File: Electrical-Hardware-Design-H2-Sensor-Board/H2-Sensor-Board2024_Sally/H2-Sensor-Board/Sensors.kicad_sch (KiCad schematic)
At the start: 28 parts, among them J4 Conn_01x03, J5 Conn_01x03, J6 Conn_01x03, J7 Conn_01x03, SW2 TARE BUTTON, U8 AD8608ARZ, U9 BME280

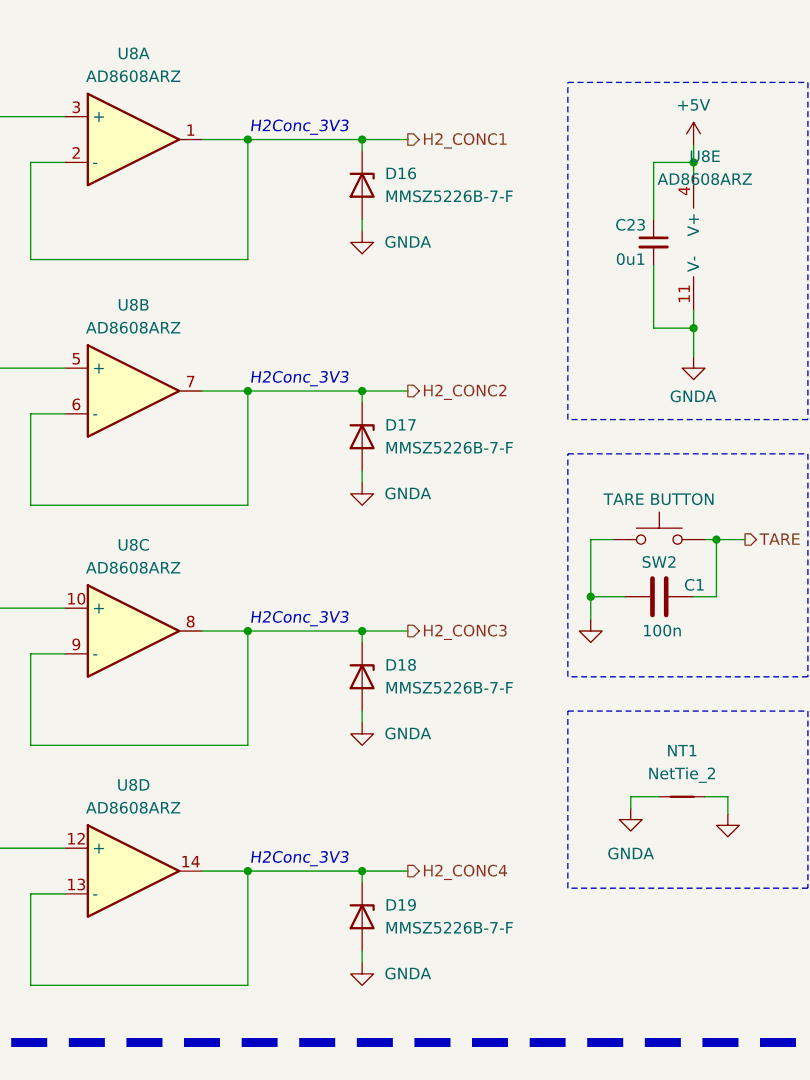
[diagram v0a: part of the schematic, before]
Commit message: reworked comparator+ADC pinout, added terminal C bank
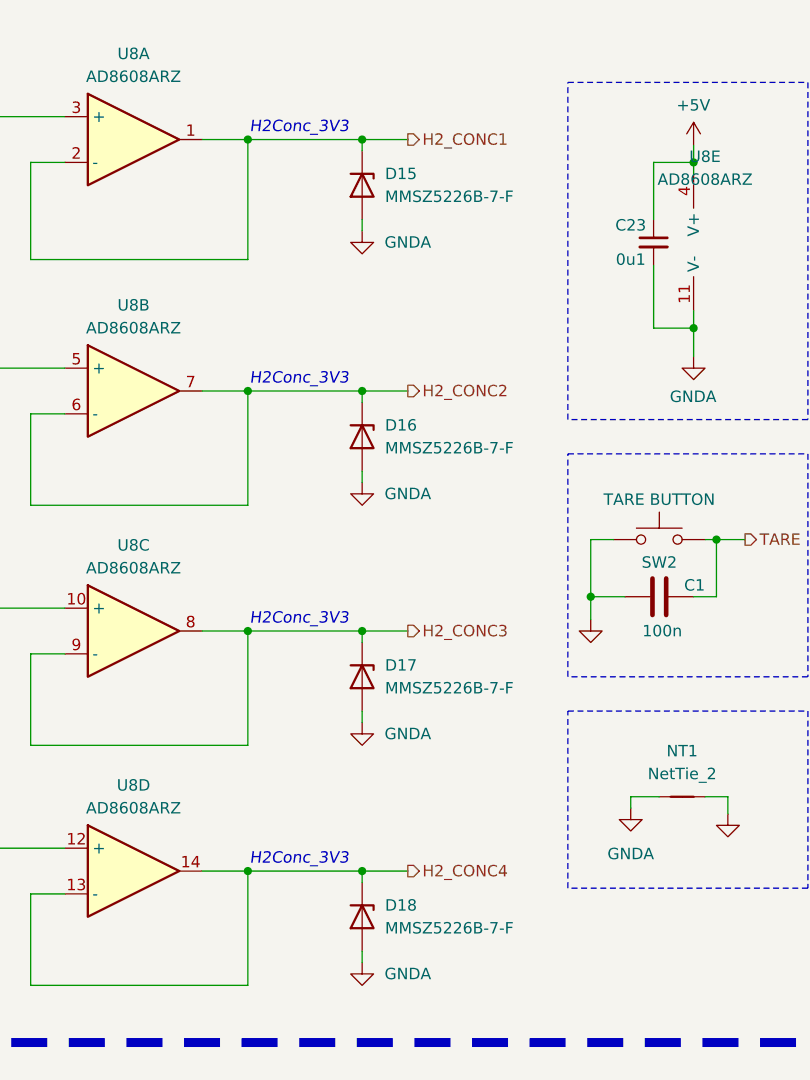
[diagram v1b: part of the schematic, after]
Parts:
- renumbered D16 to D15, D17 to D16, D18 to D17, D19 to D18
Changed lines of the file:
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@@
 		(on_board yes)
 		(dnp no)
-		(property "Reference" "#PWR044"
+		(property "Reference" "#PWR039"
 			(at 121.285 115.57 0)
 			(effects
@@
 			(project "H2 Sensor Board Lucy Rev 1"
 				(path "/61fdd4a1-2d1e-44dc-8644-252e12d35745/7173564b-4ce8-4fe4-9cf3-378e96487dfe"
-					(reference "#PWR044")
+					(reference "#PWR039")
 					(unit 1)
 				)
@@
 		(dnp no)
 		(fields_autoplaced yes)
-		(property "Reference" "D17"
+		(property "Reference" "D16"
 			(at 93.98 66.675 90)
 			(effects
@@
 			(project "H2-Sensor-Board_Sally-R1.0"
 				(path "/61fdd4a1-2d1e-44dc-8644-252e12d35745/7173564b-4ce8-4fe4-9cf3-378e96487dfe"
-					(reference "D17")
+					(reference "D16")
 					(unit 1)
 				)
@@
 		(on_board yes)
 		(dnp no)
-		(property "Reference" "#PWR035"
+		(property "Reference" "#PWR030"
 			(at 43.18 51.435 0)
 			(effects
@@
 			(project "H2 Sensor Board Lucy Rev 1"
 				(path "/61fdd4a1-2d1e-44dc-8644-252e12d35745/7173564b-4ce8-4fe4-9cf3-378e96487dfe"
-					(reference "#PWR035")
+					(reference "#PWR030")
 					(unit 1)
 				)
@@
 		(on_board yes)
 		(dnp no)
-		(property "Reference" "#PWR039"
+		(property "Reference" "#PWR034"
 			(at 91.44 51.435 0)
 			(effects
@@
 			(project "H2 Sensor Board Lucy Rev 1"
 				(path "/61fdd4a1-2d1e-44dc-8644-252e12d35745/7173564b-4ce8-4fe4-9cf3-378e96487dfe"
-					(reference "#PWR039")
+					(reference "#PWR034")
 					(unit 1)
 				)
@@
 		(on_board yes)
 		(dnp no)
-		(property "Reference" "#PWR051"
+		(property "Reference" "#PWR046"
 			(at 170.815 113.665 0)
 			(effects
@@
 			(project "H2-Sensor-Board_Sally-R1.0"
 				(path "/61fdd4a1-2d1e-44dc-8644-252e12d35745/7173564b-4ce8-4fe4-9cf3-378e96487dfe"
-					(reference "#PWR051")
+					(reference "#PWR046")
 					(unit 1)
 				)
@@
 		(on_board yes)
 		(dnp no)
-		(property "Reference" "#PWR036"
+		(property "Reference" "#PWR031"
 			(at 43.18 79.375 0)
 			(effects
@@
 			(project "H2-Sensor-Board_Sally-R1.0"
 				(path "/61fdd4a1-2d1e-44dc-8644-252e12d35745/7173564b-4ce8-4fe4-9cf3-378e96487dfe"
-					(reference "#PWR036")
+					(reference "#PWR031")
 					(unit 1)
 				)
@@
 		(on_board yes)
 		(dnp no)
-		(property "Reference" "#PWR041"
+		(property "Reference" "#PWR036"
 			(at 91.44 106.045 0)
 			(effects
@@
 			(project "H2-Sensor-Board_Sally-R1.0"
 				(path "/61fdd4a1-2d1e-44dc-8644-252e12d35745/7173564b-4ce8-4fe4-9cf3-378e96487dfe"
-					(reference "#PWR041")
+					(reference "#PWR036")
 					(unit 1)
 				)
@@
 		(on_board yes)
 		(dnp no)
-		(property "Reference" "#PWR038"
+		(property "Reference" "#PWR033"
 			(at 43.18 132.715 0)
 			(effects
@@
 			(project "H2-Sensor-Board_Sally-R1.0"
 				(path "/61fdd4a1-2d1e-44dc-8644-252e12d35745/7173564b-4ce8-4fe4-9cf3-378e96487dfe"
-					(reference "#PWR038")
+					(reference "#PWR033")
 					(unit 1)
 				)
@@
 		(dnp no)
 		(fields_autoplaced yes)
-		(property "Reference" "D18"
+		(property "Reference" "D17"
 			(at 93.98 93.345 90)
 			(effects
@@
 			(project "H2-Sensor-Board_Sally-R1.0"
 				(path "/61fdd4a1-2d1e-44dc-8644-252e12d35745/7173564b-4ce8-4fe4-9cf3-378e96487dfe"
-					(reference "D18")
+					(reference "D17")
 					(unit 1)
 				)
@@
 		(dnp no)
 		(fields_autoplaced yes)
-		(property "Reference" "#PWR054"
+		(property "Reference" "#PWR049"
 			(at 184.785 76.2 0)
 			(effects
@@
 			(project "H2 Sensor Board Lucy Rev 1"
 				(path "/61fdd4a1-2d1e-44dc-8644-252e12d35745/7173564b-4ce8-4fe4-9cf3-378e96487dfe"
-					(reference "#PWR054")
+					(reference "#PWR049")
 					(unit 1)
 				)
@@
 		(dnp no)
 		(fields_autoplaced yes)
-		(property "Reference" "#PWR056"
+		(property "Reference" "#PWR051"
 			(at 241.935 36.83 0)
 			(effects
@@
 			(project "H2 Sensor Board Lucy Rev 1"
 				(path "/61fdd4a1-2d1e-44dc-8644-252e12d35745/7173564b-4ce8-4fe4-9cf3-378e96487dfe"
-					(reference "#PWR056")
+					(reference "#PWR051")
 					(unit 1)
 				)
@@
 		(dnp no)
 		(fields_autoplaced yes)
-		(property "Reference" "D16"
+		(property "Reference" "D15"
 			(at 93.98 38.735 90)
 			(effects
@@
 			(project "H2 Sensor Board Lucy Rev 1"
 				(path "/61fdd4a1-2d1e-44dc-8644-252e12d35745/7173564b-4ce8-4fe4-9cf3-378e96487dfe"
-					(reference "D16")
+					(reference "D15")
 					(unit 1)
 				)
@@
 		(dnp no)
 		(fields_autoplaced yes)
-		(property "Reference" "#PWR053"
+		(property "Reference" "#PWR048"
 			(at 182.245 29.21 0)
 			(effects
@@
 			(project "H2 Sensor Board Lucy Rev 1"
 				(path "/61fdd4a1-2d1e-44dc-8644-252e12d35745/7173564b-4ce8-4fe4-9cf3-378e96487dfe"
-					(reference "#PWR053")
+					(reference "#PWR048")
 					(unit 1)
 				)
@@
 		(on_board yes)
 		(dnp no)
-		(property "Reference" "#PWR040"
+		(property "Reference" "#PWR035"
 			(at 91.44 79.375 0)
 			(effects
@@
 			(project "H2-Sensor-Board_Sally-R1.0"
 				(path "/61fdd4a1-2d1e-44dc-8644-252e12d35745/7173564b-4ce8-4fe4-9cf3-378e96487dfe"
-					(reference "#PWR040")
+					(reference "#PWR035")
 					(unit 1)
 				)
@@
 		(on_board yes)
 		(dnp no)
-		(property "Reference" "#PWR045"
+		(property "Reference" "#PWR040"
 			(at 128.27 39.37 0)
 			(effects
@@
 			(project ""
 				(path "/61fdd4a1-2d1e-44dc-8644-252e12d35745/7173564b-4ce8-4fe4-9cf3-378e96487dfe"
-					(reference "#PWR045")
+					(reference "#PWR040")
 					(unit 1)
 				)
@@
 		(on_board yes)
 		(dnp no)
-		(property "Reference" "#PWR042"
+		(property "Reference" "#PWR037"
 			(at 91.44 132.715 0)
 			(effects
@@
 			(project "H2-Sensor-Board_Sally-R1.0"
 				(path "/61fdd4a1-2d1e-44dc-8644-252e12d35745/7173564b-4ce8-4fe4-9cf3-378e96487dfe"
-					(reference "#PWR042")
+					(reference "#PWR037")
 					(unit 1)
 				)
@@
 		(on_board yes)
 		(dnp no)
-		(property "Reference" "#PWR057"
+		(property "Reference" "#PWR052"
 			(at 262.255 33.02 0)
 			(effects
@@
 			(project "H2 Sensor Board Lucy Rev 1"
 				(path "/61fdd4a1-2d1e-44dc-8644-252e12d35745/7173564b-4ce8-4fe4-9cf3-378e96487dfe"
-					(reference "#PWR057")
+					(reference "#PWR052")
 					(unit 1)
 				)
@@
 		(on_board yes)
 		(dnp no)
-		(property "Reference" "#PWR037"
+		(property "Reference" "#PWR032"
 			(at 43.18 106.045 0)
 			(effects
@@
 			(project "H2-Sensor-Board_Sally-R1.0"
 				(path "/61fdd4a1-2d1e-44dc-8644-252e12d35745/7173564b-4ce8-4fe4-9cf3-378e96487dfe"
-					(reference "#PWR037")
+					(reference "#PWR032")
 					(unit 1)
 				)
@@
 			(project "H2 Sensor Board Lucy Rev 1"
 				(path "/61fdd4a1-2d1e-44dc-8644-252e12d35745/7173564b-4ce8-4fe4-9cf3-378e96487dfe"
-					(reference "#PWR043")
+					(reference "#PWR038")
 					(unit 1)
 				)
@@
 		(dnp no)
 		(fields_autoplaced yes)
-		(property "Reference" "#PWR058"
+		(property "Reference" "#PWR053"
 			(at 269.875 22.86 0)
 			(effects
@@
 			(project "H2 Sensor Board Lucy Rev 1"
 				(path "/61fdd4a1-2d1e-44dc-8644-252e12d35745/7173564b-4ce8-4fe4-9cf3-378e96487dfe"
-					(reference "#PWR058")
+					(reference "#PWR053")
 					(unit 1)
 				)
@@
 		(on_board yes)
 		(dnp no)
-		(property "Reference" "#PWR049"
+		(property "Reference" "#PWR044"
 			(at 170.815 88.265 0)
 			(effects
@@
 			(project "H2 Sensor Board Lucy Rev 1"
 				(path "/61fdd4a1-2d1e-44dc-8644-252e12d35745/7173564b-4ce8-4fe4-9cf3-378e96487dfe"
-					(reference "#PWR049")
+					(reference "#PWR044")
 					(unit 1)
 				)
@@
 		(dnp no)
 		(fields_autoplaced yes)
-		(property "Reference" "D19"
+		(property "Reference" "D18"
 			(at 93.98 120.015 90)
 			(effects
@@
 			(project "H2-Sensor-Board_Sally-R1.0"
 				(path "/61fdd4a1-2d1e-44dc-8644-252e12d35745/7173564b-4ce8-4fe4-9cf3-378e96487dfe"
-					(reference "D19")
+					(reference "D18")
 					(unit 1)
 				)
@@
 			(project "H2 Sensor Board Lucy Rev 1"
 				(path "/61fdd4a1-2d1e-44dc-8644-252e12d35745/7173564b-4ce8-4fe4-9cf3-378e96487dfe"
-					(reference "#PWR047")
+					(reference "#PWR042")
 					(unit 1)
 				)
@@
 		(dnp no)
 		(fields_autoplaced yes)
-		(property "Reference" "#PWR048"
+		(property "Reference" "#PWR043"
 			(at 163.195 43.18 0)
 			(effects
@@
 			(project "H2 Sensor Board Lucy Rev 1"
 				(path "/61fdd4a1-2d1e-44dc-8644-252e12d35745/7173564b-4ce8-4fe4-9cf3-378e96487dfe"
-					(reference "#PWR048")
+					(reference "#PWR043")
 					(unit 1)
 				)
@@
 		(dnp no)
 		(fields_autoplaced yes)
-		(property "Reference" "#PWR055"
+		(property "Reference" "#PWR050"
 			(at 208.915 43.18 0)
 			(effects
@@
 			(project "H2 Sensor Board Lucy Rev 1"
 				(path "/61fdd4a1-2d1e-44dc-8644-252e12d35745/7173564b-4ce8-4fe4-9cf3-378e96487dfe"
-					(reference "#PWR055")
+					(reference "#PWR050")
 					(unit 1)
 				)
@@
 		(on_board yes)
 		(dnp no)
-		(property "Reference" "#PWR046"
+		(property "Reference" "#PWR041"
 			(at 128.27 65.405 0)
 			(effects
@@
 			(project ""
 				(path "/61fdd4a1-2d1e-44dc-8644-252e12d35745/7173564b-4ce8-4fe4-9cf3-378e96487dfe"
-					(reference "#PWR046")
+					(reference "#PWR041")
 					(unit 1)
 				)
@@
 		(on_board yes)
 		(dnp no)
-		(property "Reference" "#PWR052"
+		(property "Reference" "#PWR047"
 			(at 170.815 126.365 0)
 			(effects
@@
 			(project "H2-Sensor-Board_Sally-R1.0"
 				(path "/61fdd4a1-2d1e-44dc-8644-252e12d35745/7173564b-4ce8-4fe4-9cf3-378e96487dfe"
-					(reference "#PWR052")
+					(reference "#PWR047")
 					(unit 1)
 				)
@@
 		(on_board yes)
 		(dnp no)
-		(property "Reference" "#PWR050"
+		(property "Reference" "#PWR045"
 			(at 170.815 100.965 0)
 			(effects
@@
 			(project "H2-Sensor-Board_Sally-R1.0"
 				(path "/61fdd4a1-2d1e-44dc-8644-252e12d35745/7173564b-4ce8-4fe4-9cf3-378e96487dfe"
-					(reference "#PWR050")
+					(reference "#PWR045")
 					(unit 1)
 				)

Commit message: layout update
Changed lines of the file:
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@@
 	(text "MQ-8 Hydrogen Sensing"
 		(exclude_from_sim no)
-		(at 15.24 16.002 0)
+		(at 15.24 16.51 0)
 		(effects
 			(font
